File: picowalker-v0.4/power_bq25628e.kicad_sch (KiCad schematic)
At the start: 0 parts

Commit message: v0.4: schematic laid out first draft
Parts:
- added C25, C27, C28, C33: 10u, Capacitor_SMD:C_0603_1608Metric, symbol Device:C
- added C26: 4.7u, Capacitor_SMD:C_0603_1608Metric, symbol Device:C
- added C29, C30: 47u, Capacitor_SMD:C_0805_2012Metric, symbol Device:C
- added C31: 47n, Capacitor_SMD:C_0402_1005Metric, symbol Device:C
- added C32: 0.1u, Capacitor_SMD:C_0402_1005Metric, symbol Device:C
- added C34: 4.7u, Capacitor_SMD:C_0402_1005Metric, symbol Device:C
- added D1: ~{STAT}, LED_SMD:LED_0402_1005Metric, symbol Device:LED
- added IC1: RT6150B-33GQW, symbol picowalker:RT6150B-33GQW
- added L2: 1.1u, Inductor_SMD:L_0402_1005Metric, symbol Device:L
- added L3: 2.2u, Inductor_SMD:L_0805_2012Metric, symbol Device:L
- added R19, R21: 5.1k, Resistor_SMD:R_0402_1005Metric, symbol Device:R
- added R20, R23, R24: 30k, Resistor_SMD:R_0603_1608Metric, symbol Device:R
- added R22: 1k, Resistor_SMD:R_0402_1005Metric, symbol Device:R
- added TH1: 10k, symbol Device:Thermistor_NTC
- added TP2: ~{QON}, TestPoint:TestPoint_Pad_1.0x1.0mm, symbol Connector:TestPoint
- added U6: BQ25628ERYKR, symbol picowalker:BQ25628ERYKR
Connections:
- new net: C31.1, L2.1, U6.16 (SW)
- new net: C31.2, U6.1 (BTST)
- new net: IC1.4 (LX1), L3.1
- new net: IC1.2 (LX2), L3.2
- new net: TP2.1, U6.7 (~{QON})
- new net: IC1.7 (PS), R24.1
- new net: D1.2 (A), R22.2
- new net: C32.1, C33.1, U6.17 (PMID)
- new net: C34.1, U6.2 (REGN)
- new net: R21.1, U6.4 (ILIM)
- new net +3.3V: C30.1, IC1.1 (VOUT), IC1.10 (FB), R22.1
- new net 3V3_EN: IC1.6 (EN), R23.2
- new net BAT+: C25.1, U6.8 (BAT+)
- new net GND: C25.2, C26.2, C27.2, C28.2, C29.2, C30.2, C32.2, C33.2, C34.2, IC1.11 (GND_PAD), IC1.3 (GND), IC1.9 (GND), R20.2, R21.2, R24.2, TH1.2, U6.15 (GND)
- new net SCL: U6.13 (SCL)
- new net SDA: U6.12 (SDA)
- new net STAT: U6.10 (STAT)
- new net TS: R19.2, R20.1, TH1.1, U6.6 (TS)
- new net TS_BIAS: R19.1, U6.5 (TS_BIAS)
- new net VBUS: C26.1, U6.18 (VBUS)
- new net VSYS: C27.1, C28.1, C29.1, IC1.5 (VIN), IC1.8 (VINA), L2.2, R23.1, U6.9 (SYS)
- new net ~{CE}: U6.14 (~{CE})
- new net ~{INT}: U6.11 (~{INT})
- new net ~{PG}: U6.3 (~{PG})
- new net ~{STAT}: D1.1 (K)
- no-connect marks 0 -> 1
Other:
- note added: "Consider swapping for 0.1u"
- note added: "Datasheet recommends: CVBUS > 1u CPMID > 10u CSYS > 20u CBAT > 10u"
- note added: "Datasheet: 30.1k"
- note added: "Datasheet: 5.32k"
- note added: "I_ILIM = K_ILIM/R_ILIM K_ILIM = 2500 +/-250 5.1k = 490 mA"

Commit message: v0.4: more rationalisation
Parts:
- C25: value 10u -> 4.7u; footprint Capacitor_SMD:C_0603_1608Metric -> Capacitor_SMD:C_0402_1005Metric
- C26: footprint Capacitor_SMD:C_0603_1608Metric -> Capacitor_SMD:C_0402_1005Metric
- R23, R24: value 30k -> 0R
- TP2: now left out of the parts list
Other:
- note added: "I think stuck at 47n. Its a bootstrap so keep to recommended."
- note removed: "Consider swapping for 0.1u"
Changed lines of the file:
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@@
 		)
 	)
-	(text "Consider swapping for 0.1u"
+	(text "I think stuck at 47n.\nIts a bootstrap so keep to recommended."
 		(exclude_from_sim no)
-		(at 153.924 90.424 0)
+		(at 94.996 69.85 0)
 		(effects
 			(font
 				(size 2 2)
 			)
+			(justify left)
 		)
 	)
@@
 		(unit 1)
 		(exclude_from_sim no)
-		(in_bom yes)
+		(in_bom no)
 		(on_board yes)
 		(dnp no)
@@
 			)
 		)
-		(property "Value" "10u"
+		(property "Value" "4.7u"
 			(at 44.45 39.3699 0)
 			(effects
@@
 			)
 		)
-		(property "Footprint" "Capacitor_SMD:C_0603_1608Metric"
+		(property "Footprint" "Capacitor_SMD:C_0402_1005Metric"
 			(at 41.6052 41.91 0)
 			(effects
@@
 			)
 		)
-		(property "Footprint" "Capacitor_SMD:C_0603_1608Metric"
+		(property "Footprint" "Capacitor_SMD:C_0402_1005Metric"
 			(at 58.1152 41.91 0)
 			(effects
@@
 			)
 		)
-		(property "Value" "30k"
+		(property "Value" "0R"
 			(at 190.5 95.2499 0)
 			(effects
@@
 			)
 		)
-		(property "Value" "30k"
+		(property "Value" "0R"
 			(at 199.39 110.4899 0)
 			(effects

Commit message: v0.4: first rough placement of PCB
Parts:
- removed R23, R24: 0R, Resistor_SMD:R_0603_1608Metric, symbol Device:R
- IC1: footprint (none) -> picowalker:SON50P250X250X80-11N-D
- TH1: footprint (none) -> picowalker:R_0402_1005Metric_Sunken
- U6: footprint (none) -> picowalker:BQ25628ERYKR
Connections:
- net 3V3_EN is gone; now on net VSYS: IC1.6 (EN)
- net GND: now also IC1.7 (PS)
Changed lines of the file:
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@@
 	(wire
 		(pts
-			(xy 193.04 97.79) (xy 193.04 99.06)
+			(xy 193.04 81.28) (xy 193.04 99.06)
 		)
 		(stroke
@@
 	(wire
 		(pts
-			(xy 201.93 105.41) (xy 201.93 101.6)
+			(xy 201.93 101.6) (xy 201.93 115.57)
 		)
 		(stroke
@@
 	(wire
 		(pts
-			(xy 193.04 81.28) (xy 193.04 90.17)
-		)
-		(stroke
-			(width 0)
-			(type default)
-		)
-	)
-	(wire
-		(pts
 			(xy 232.41 88.9) (xy 236.22 88.9)
 		)
@@
 	(wire
 		(pts
-			(xy 201.93 113.03) (xy 201.93 115.57)
-		)
-		(stroke
-			(width 0)
-			(type default)
-		)
-	)
-	(wire
-		(pts
 			(xy 124.46 123.19) (xy 124.46 124.46)
 		)
@@
 		)
 	)
+	(label "PS"
+		(at 201.93 101.6 0)
+		(effects
+			(font
+				(size 1.27 1.27)
+			)
+			(justify left bottom)
+		)
+	)
 	(label "~{STAT}"
 		(at 91.44 184.15 90)
@@
 			)
 		)
-		(property "Footprint" ""
+		(property "Footprint" "picowalker:R_0402_1005Metric_Sunken"
 			(at 59.69 167.64 0)
 			(effects
@@
 			)
 		)
-		(property "Footprint" ""
+		(property "Footprint" "picowalker:SON50P250X250X80-11N-D"
 			(at 220.98 77.47 0)
 			(effects
@@
 			)
 		)
-		(property "Footprint" ""
+		(property "Footprint" "picowalker:BQ25628ERYKR"
 			(at 100.33 80.01 0)
 			(effects
@@
 	(symbol
 		(lib_id "Device:R")
-		(at 193.04 93.98 0)
-		(mirror y)
-		(unit 1)
-		(exclude_from_sim no)
-		(in_bom yes)
-		(on_board yes)
-		(dnp no)
-		(property "Reference" "R23"
-			(at 190.5 92.7099 0)
-			(effects
-				(font
-					(size 1.27 1.27)
-				)
-				(justify left)
-			)
-		)
-		(property "Value" "0R"
-			(at 190.5 95.2499 0)
-			(effects
-				(font
-					(size 1.27 1.27)
-				)
-				(justify left)
-			)
-		)
-		(property "Footprint" "Resistor_SMD:R_0603_1608Metric"
-			(at 194.818 93.98 90)
-			(effects
-				(font
-					(size 1.27 1.27)
-				)
-				(hide yes)
-			)
-		)
-		(property "Datasheet" "~"
-			(at 193.04 93.98 0)
-			(effects
-				(font
-					(size 1.27 1.27)
-				)
-				(hide yes)
-			)
-		)
-		(property "Description" "Resistor"
-			(at 193.04 93.98 0)
-			(effects
-				(font
-					(size 1.27 1.27)
-				)
-				(hide yes)
-			)
-		)
-		(pin "1"
-		)
-		(pin "2"
-		)
-		(instances
-			(project "picowalker-v0.4"
-				(path "/aa8773bf-a88b-4bf9-9961-8e312cd9d0e3/f9bb3943-6d25-47dd-92d4-668afa6f251a"
-					(reference "R23")
-					(unit 1)
-				)
-			)
-		)
-	)
-	(symbol
-		(lib_id "Device:R")
 		(at 91.44 165.1 0)
 		(mirror y)
@@
 					(unit 1)
 				)
-			)
-		)
-	)
-	(symbol
-		(lib_id "Device:R")
-		(at 201.93 109.22 0)
-		(mirror y)
-		(unit 1)
-		(exclude_from_sim no)
-		(in_bom yes)
-		(on_board yes)
-		(dnp no)
-		(property "Reference" "R24"
-			(at 199.39 107.9499 0)
-			(effects
-				(font
-					(size 1.27 1.27)
-				)
-				(justify left)
-			)
-		)
-		(property "Value" "0R"
-			(at 199.39 110.4899 0)
-			(effects
-				(font
-					(size 1.27 1.27)
-				)
-				(justify left)
-			)
-		)
-		(property "Footprint" "Resistor_SMD:R_0603_1608Metric"
-			(at 203.708 109.22 90)
-			(effects
-				(font
-					(size 1.27 1.27)
-				)
-				(hide yes)
-			)
-		)
-		(property "Datasheet" "~"
-			(at 201.93 109.22 0)
-			(effects
-				(font
-					(size 1.27 1.27)
-				)
-				(hide yes)
-			)
-		)
-		(property "Description" "Resistor"
-			(at 201.93 109.22 0)
-			(effects
-				(font
-					(size 1.27 1.27)
-				)
-				(hide yes)
-			)
-		)
-		(pin "1"
-		)
-		(pin "2"
-		)
-		(instances
-			(project "picowalker-v0.4"
-				(path "/aa8773bf-a88b-4bf9-9961-8e312cd9d0e3/f9bb3943-6d25-47dd-92d4-668afa6f251a"
-					(reference "R24")
-					(unit 1)
-				)

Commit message: v0.4: good start on routing
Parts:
- added TP1: ~{PG}, picowalker:TestPoint_Pad_D1.0mm_Nosilk, symbol Connector:TestPoint
- L2: footprint Inductor_SMD:L_0402_1005Metric -> Inductor_SMD:L_0603_1608Metric
- TP2: footprint TestPoint:TestPoint_Pad_1.0x1.0mm -> picowalker:TestPoint_Pad_D1.0mm_Nosilk
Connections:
- net ~{PG}: now also TP1.1
- net SW: now reaches C31.1, L2.1, U6.16 (SW)
- net ~{QON}: now reaches TP2.1, U6.7 (~{QON})
- net PMID: now reaches C32.1, C33.1, U6.17 (PMID)
- net SCL renamed I2C.SCL
- net SDA renamed I2C.SDA
- no-connect marks 1 -> 0
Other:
- moved on the sheet: TP2
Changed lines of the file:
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@@
 		)
 	)
-	(text_box "Unused outputs"
+	(text_box "Unused pins"
 		(exclude_from_sim no)
 		(at 111.76 144.78 0)
@@
 		(color 0 0 0 0)
 	)
-	(no_connect
-		(at 127 157.48)
-	)
 	(bus_entry
 		(at 68.58 91.44)
@@
 	(wire
 		(pts
-			(xy 62.23 101.6) (xy 62.23 100.33)
-		)
-		(stroke
-			(width 0)
-			(type default)
-		)
-	)
-	(wire
-		(pts
 			(xy 232.41 81.28) (xy 236.22 81.28)
 		)
@@
 	(wire
 		(pts
+			(xy 138.43 170.18) (xy 125.73 170.18)
+		)
+		(stroke
+			(width 0)
+			(type default)
+		)
+	)
+	(wire
+		(pts
 			(xy 91.44 177.8) (xy 91.44 184.15)
 		)
@@
 	(wire
 		(pts
-			(xy 83.82 101.6) (xy 62.23 101.6)
-		)
-		(stroke
-			(width 0)
-			(type default)
-		)
-	)
-	(wire
-		(pts
 			(xy 218.44 113.03) (xy 218.44 115.57)
 		)
@@
 		(pts
 			(xy 209.55 83.82) (xy 200.66 83.82)
+		)
+		(stroke
+			(width 0)
+			(type default)
+		)
+	)
+	(wire
+		(pts
+			(xy 66.04 101.6) (xy 83.82 101.6)
 		)
 		(stroke
@@
 		)
 	)
+	(label "SW"
+		(at 119.38 83.82 0)
+		(effects
+			(font
+				(size 1.27 1.27)
+			)
+			(justify left bottom)
+		)
+	)
 	(label "PS"
 		(at 201.93 101.6 0)
@@
 		)
 	)
+	(label "PMID"
+		(at 120.65 114.3 0)
+		(effects
+			(font
+				(size 1.27 1.27)
+			)
+			(justify left bottom)
+		)
+	)
 	(label "~{STAT}"
 		(at 91.44 184.15 90)
@@
 		)
 	)
+	(label "~{QON}"
+		(at 138.43 170.18 180)
+		(effects
+			(font
+				(size 1.27 1.27)
+			)
+			(justify right bottom)
+		)
+	)
+	(label "~{QON}"
+		(at 66.04 101.6 0)
+		(effects
+			(font
+				(size 1.27 1.27)
+			)
+			(justify left bottom)
+		)
+	)
 	(label "STAT"
 		(at 127 106.68 180)
@@
 		)
 	)
-	(label "SDA"
+	(label "I2C.SDA"
 		(at 73.66 91.44 0)
 		(effects
@@
 		)
 	)
-	(label "SCL"
+	(label "I2C.SCL"
 		(at 73.66 93.98 0)
 		(effects
@@
 			)
 		)
-		(property "Footprint" "Inductor_SMD:L_0402_1005Metric"
+		(property "Footprint" "Inductor_SMD:L_0603_1608Metric"
 			(at 133.35 83.82 0)
 			(effects
@@
 	)
 	(symbol
+		(lib_id "Connector:TestPoint")
+		(at 127 157.48 0)
+		(unit 1)
+		(exclude_from_sim no)
+		(in_bom yes)
+		(on_board yes)
+		(dnp no)
+		(fields_autoplaced yes)
+		(property "Reference" "TP1"
+			(at 129.54 152.9079 0)
+			(effects
+				(font
+					(size 1.27 1.27)
+				)
+				(justify left)
+			)
+		)
+		(property "Value" "~{PG}"
+			(at 129.54 155.4479 0)
+			(effects
+				(font
+					(size 1.27 1.27)
+				)
+				(justify left)
+			)
+		)
+		(property "Footprint" "picowalker:TestPoint_Pad_D1.0mm_Nosilk"
+			(at 132.08 157.48 0)
+			(effects
+				(font
+					(size 1.27 1.27)
+				)
+				(hide yes)
+			)
+		)
+		(property "Datasheet" "~"
+			(at 132.08 157.48 0)
+			(effects
+				(font
+					(size 1.27 1.27)
+				)
+				(hide yes)
+			)
+		)
+		(property "Description" "test point"
+			(at 127 157.48 0)
+			(effects
+				(font
+					(size 1.27 1.27)
+				)
+				(hide yes)
+			)
+		)
+		(pin "1"
+		)
+		(instances
+			(project ""
+				(path "/aa8773bf-a88b-4bf9-9961-8e312cd9d0e3/f9bb3943-6d25-47dd-92d4-668afa6f251a"
+					(reference "TP1")
+					(unit 1)
+				)
+			)
+		)
+	)
+	(symbol
 		(lib_id "power:GND")
 		(at 148.59 127 0)
@@
 	(symbol
 		(lib_id "Connector:TestPoint")
-		(at 62.23 100.33 0)
+		(at 125.73 170.18 0)
 		(unit 1)
 		(exclude_from_sim no)
@@
 		(dnp no)
 		(property "Reference" "TP2"
-			(at 59.69 95.7579 0)
+			(at 123.19 165.6079 0)
 			(effects
 				(font
@@
 		)
 		(property "Value" "~{QON}"
-			(at 59.69 98.2979 0)
+			(at 123.19 168.1479 0)
 			(effects
 				(font
@@
 			)
 		)
-		(property "Footprint" "TestPoint:TestPoint_Pad_1.0x1.0mm"
-			(at 67.31 100.33 0)
+		(property "Footprint" "picowalker:TestPoint_Pad_D1.0mm_Nosilk"
+			(at 130.81 170.18 0)
 			(effects
 				(font
@@
 		)
 		(property "Datasheet" "~"
-			(at 67.31 100.33 0)
+			(at 130.81 170.18 0)
 			(effects
 				(font
@@
 		)
 		(property "Description" "test point"
-			(at 62.23 100.33 0)
+			(at 125.73 170.18 0)
 			(effects
 				(font
@@
 		)
 		(instances
-			(project ""
+			(project "picowalker-v0.4"
 				(path "/aa8773bf-a88b-4bf9-9961-8e312cd9d0e3/f9bb3943-6d25-47dd-92d4-668afa6f251a"
 					(reference "TP2")

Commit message: v0.4: running DRC checks
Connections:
- net STAT is gone; now on net ~{STAT}: U6.10 (STAT)
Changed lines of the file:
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@@
 		)
 	)
-	(label "STAT"
+	(label "~{STAT}"
 		(at 127 106.68 180)
 		(effects

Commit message: v0.4: idk, minimal changes
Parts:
- removed IC1: RT6150B-33GQW, picowalker:SON50P250X250X80-11N-D, symbol picowalker:RT6150B-33GQW
- added U9: RT6150B-33GQW, picowalker:SON50P250X250X80-11N-D, symbol picowalker:RT6150B-33GQW
- TP1: now left out of the parts list
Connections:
- net +3.3V: now also U9.1 (VOUT), U9.10 (FB)
- net GND: now also U9.11 (GND_PAD), U9.3 (GND), U9.7 (PS), U9.9 (GND)
- net VSYS: now also U9.5 (VIN), U9.6 (EN), U9.8 (VINA)
- net at L3.1: now also U9.4 (LX1)
- net at L3.2: now also U9.2 (LX2)

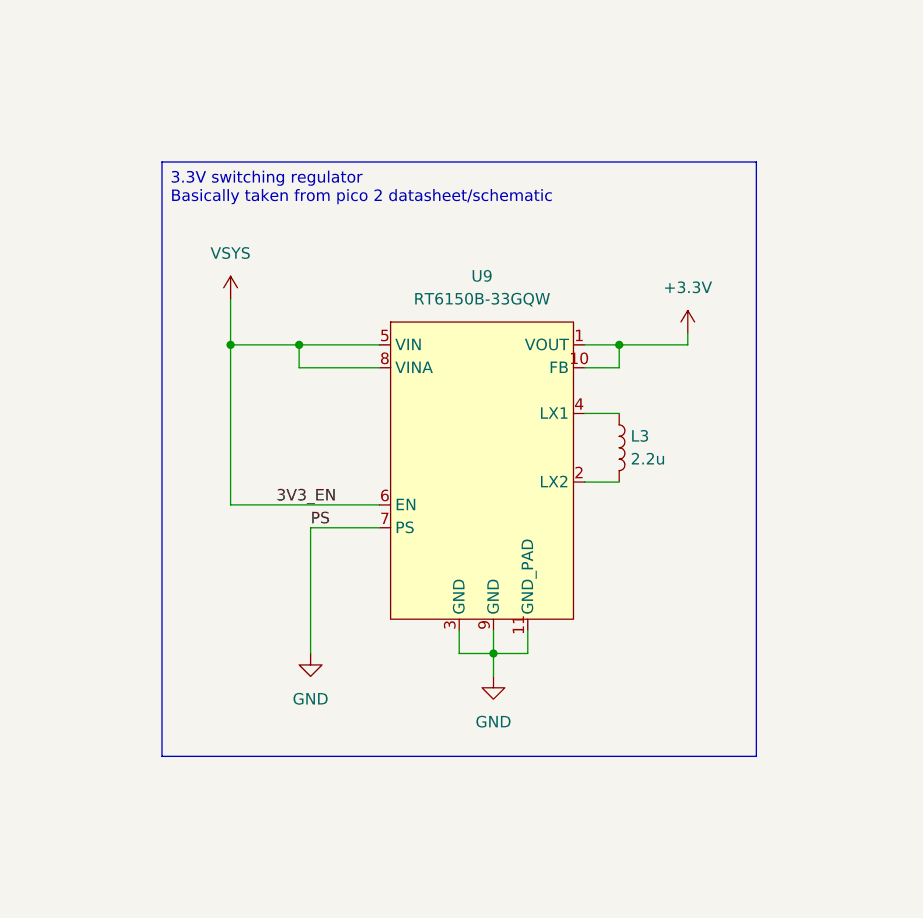
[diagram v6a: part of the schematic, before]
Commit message: v0.4: add test points for touch pad
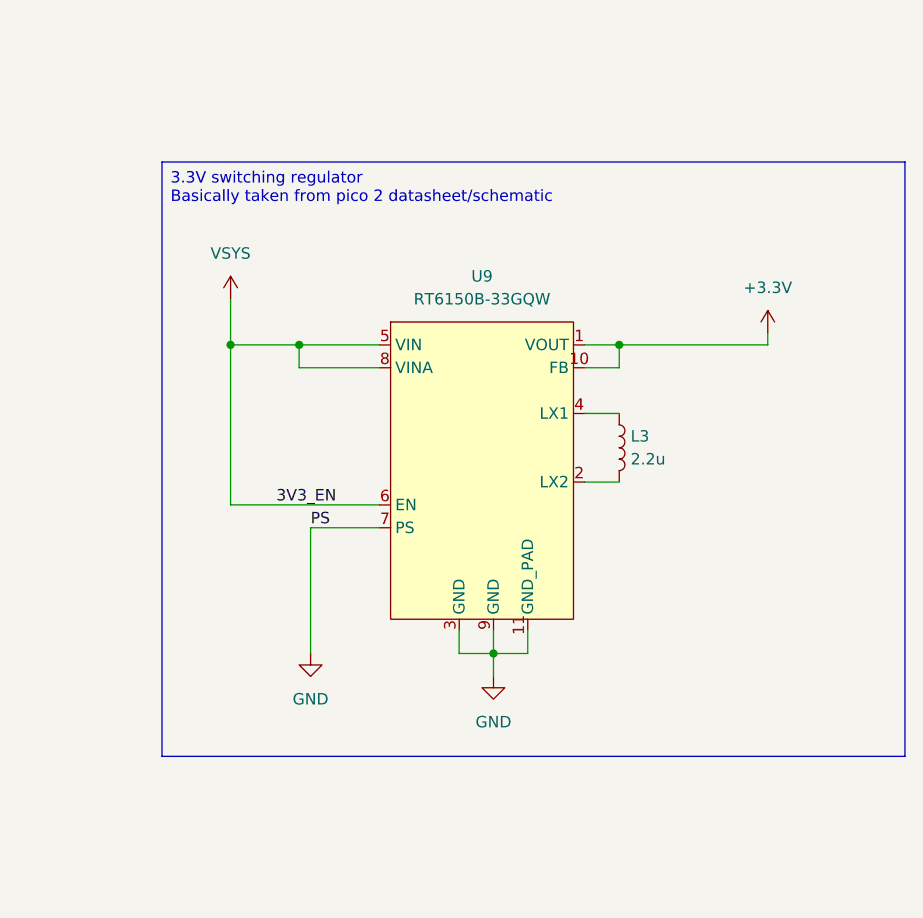
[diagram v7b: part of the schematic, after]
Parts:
- TH1: footprint picowalker:R_0402_1005Metric_Sunken -> Resistor_SMD:R_0402_1005Metric
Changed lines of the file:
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@@
 		(exclude_from_sim no)
 		(at 185.42 60.96 0)
-		(size 66.04 66.04)
+		(size 82.55 66.04)
 		(margins 0.9525 0.9525 0.9525 0.9525)
 		(stroke
@@
 	(wire
 		(pts
-			(xy 236.22 81.28) (xy 243.84 81.28)
-		)
-		(stroke
-			(width 0)
-			(type default)
-		)
-	)
-	(wire
-		(pts
-			(xy 243.84 81.28) (xy 243.84 80.01)
+			(xy 236.22 81.28) (xy 252.73 81.28)
+		)
+		(stroke
+			(width 0)
+			(type default)
+		)
+	)
+	(wire
+		(pts
+			(xy 252.73 81.28) (xy 252.73 80.01)
 		)
 		(stroke
@@
 	(symbol
 		(lib_id "power:+3.3V")
-		(at 243.84 80.01 0)
+		(at 252.73 80.01 0)
 		(unit 1)
 		(exclude_from_sim no)
@@
 		(fields_autoplaced yes)
 		(property "Reference" "#PWR073"
-			(at 243.84 83.82 0)
+			(at 252.73 83.82 0)
 			(effects
 				(font
@@
 		)
 		(property "Value" "+3.3V"
-			(at 243.84 74.93 0)
+			(at 252.73 74.93 0)
 			(effects
 				(font
@@
 		)
 		(property "Footprint" ""
-			(at 243.84 80.01 0)
+			(at 252.73 80.01 0)
 			(effects
 				(font
@@
 		)
 		(property "Datasheet" ""
-			(at 243.84 80.01 0)
+			(at 252.73 80.01 0)
 			(effects
 				(font
@@
 		)
 		(property "Description" "Power symbol creates a global label with name \"+3.3V\""
-			(at 243.84 80.01 0)
+			(at 252.73 80.01 0)
 			(effects
 				(font
@@
 			)
 		)
-		(property "Footprint" "picowalker:R_0402_1005Metric_Sunken"
+		(property "Footprint" "Resistor_SMD:R_0402_1005Metric"
 			(at 59.69 167.64 0)
 			(effects

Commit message: v0.4: send to manufacture
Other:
- note added: "PS low = power save mode (unknown switching method) PS high = PWM mode @ 1 MHz"
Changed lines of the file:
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@@
+		)
+	)
+	(text "PS low = power save mode (unknown switching method)\nPS high = PWM mode @ 1 MHz"
+		(exclude_from_sim no)
+		(at 214.122 130.302 0)
+		(effects
+			(font
+				(size 1.27 1.27)
+			)
 		)
 	)
